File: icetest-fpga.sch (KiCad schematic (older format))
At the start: 26 parts, among them J1 R, J2 R, J3 R

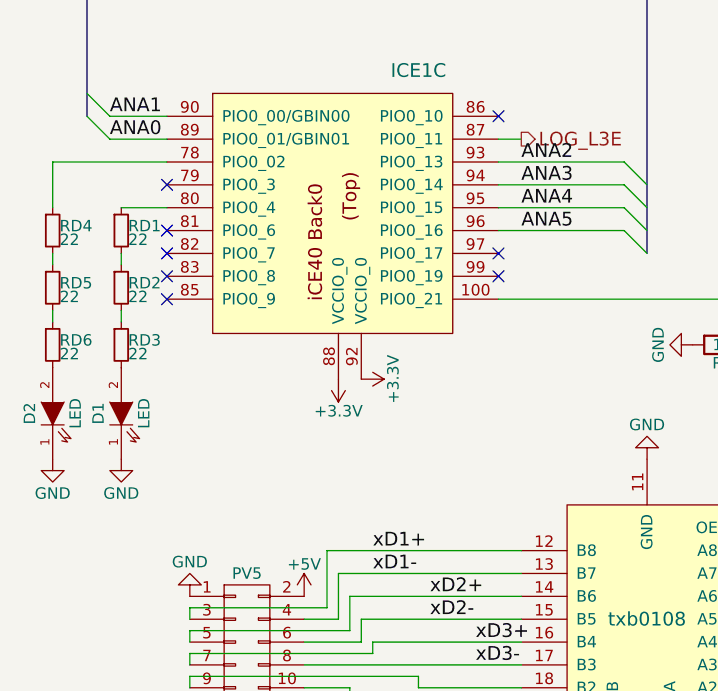
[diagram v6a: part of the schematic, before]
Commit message: more current for LEDs
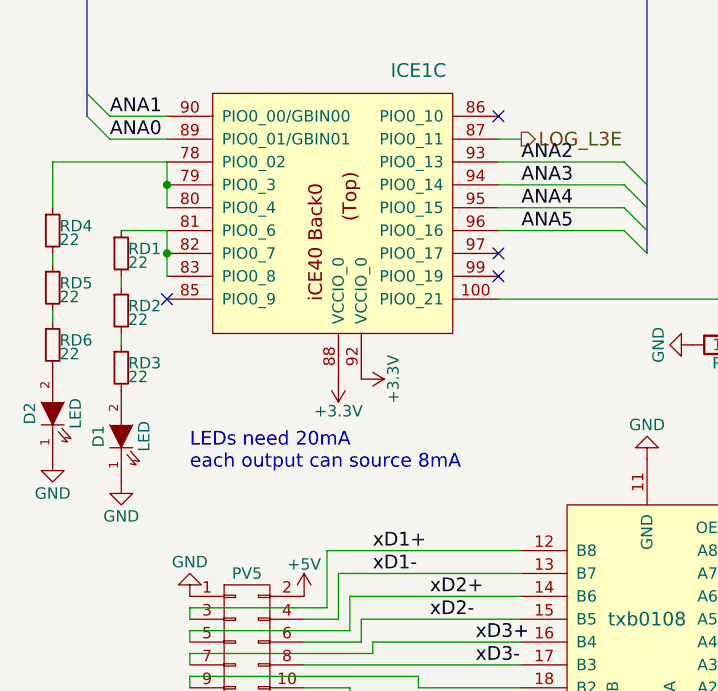
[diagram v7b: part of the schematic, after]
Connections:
- net at ICE1.78 (PIO0_02), RD4.1: now also ICE1.79 (PIO0_3), ICE1.80 (PIO0_4)
- net at RD1.1: now also ICE1.81 (PIO0_6), ICE1.82 (PIO0_7), ICE1.83 (PIO0_8); no longer ICE1.80 (PIO0_4)
- no-connect marks 31 -> 27
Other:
- note added: "LEDs need 20mA\neach output can source 8mA"
- moved on the sheet: D1, RD1, RD2, RD3
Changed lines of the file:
@@
 NoConn ~ 2650 4300
 NoConn ~ 2650 4400
-NoConn ~ 1200 4000
-NoConn ~ 1200 4200
-NoConn ~ 1200 4300
 NoConn ~ 1200 4500
 Text Label 6200 5400 0    60   ~ 0
@@
 	4700 2300 4950 2300
 NoConn ~ 6400 3350
-NoConn ~ 1200 4400
 Wire Wire Line
 	2750 3800 2650 3800
@@
 L LED D1
 U 1 1 578DAD29
-P 1000 5000
-F 0 "D1" H 1000 5100 50  0000 C CNN
-F 1 "LED" H 1000 4900 50  0000 C CNN
-F 2 "local:D_0603_HandSoldering" H 1000 5000 50  0001 C CNN
-F 3 "" H 1000 5000 50  0000 C CNN
-	1    1000 5000
+P 1000 5100
+F 0 "D1" H 1000 5200 50  0000 C CNN
+F 1 "LED" H 1000 5000 50  0000 C CNN
+F 2 "local:D_0603_HandSoldering" H 1000 5100 50  0001 C CNN
+F 3 "" H 1000 5100 50  0000 C CNN
+	1    1000 5100
 	0    -1   -1   0
 $EndComp
@@
 L GND #PWR072
 U 1 1 578DB32E
-P 1000 5200
-F 0 "#PWR072" H 1000 4950 50  0001 C CNN
-F 1 "GND" H 1000 5050 50  0000 C CNN
-F 2 "" H 1000 5200 50  0000 C CNN
-F 3 "" H 1000 5200 50  0000 C CNN
-	1    1000 5200
-	1    0    0    -1
-$EndComp
-Wire Wire Line
-	1200 4100 1000 4100
-Wire Wire Line
-	1000 4600 1000 4550
-Wire Wire Line
-	1000 4350 1000 4300
+P 1000 5300
+F 0 "#PWR072" H 1000 5050 50  0001 C CNN
+F 1 "GND" H 1000 5150 50  0000 C CNN
+F 2 "" H 1000 5300 50  0000 C CNN
+F 3 "" H 1000 5300 50  0000 C CNN
+	1    1000 5300
+	1    0    0    -1
+$EndComp
+Wire Wire Line
+	1000 4700 1000 4650
+Wire Wire Line
+	1000 4450 1000 4400
 $Comp
 L R_Small RD2
 U 1 1 578DAF76
-P 1000 4450
-F 0 "RD2" H 1030 4470 50  0000 L CNN
-F 1 "22" H 1030 4410 50  0000 L CNN
-F 2 "Resistors_SMD:R_0603_HandSoldering" H 1000 4450 50  0001 C CNN
-F 3 "" H 1000 4450 50  0000 C CNN
-	1    1000 4450
+P 1000 4550
+F 0 "RD2" H 1030 4570 50  0000 L CNN
+F 1 "22" H 1030 4510 50  0000 L CNN
+F 2 "Resistors_SMD:R_0603_HandSoldering" H 1000 4550 50  0001 C CNN
+F 3 "" H 1000 4550 50  0000 C CNN
+	1    1000 4550
 	1    0    0    -1
 $EndComp
@@
 L R_Small RD3
 U 1 1 578DAFC3
-P 1000 4700
-F 0 "RD3" H 1030 4720 50  0000 L CNN
-F 1 "22" H 1030 4660 50  0000 L CNN
-F 2 "Resistors_SMD:R_0603_HandSoldering" H 1000 4700 50  0001 C CNN
-F 3 "" H 1000 4700 50  0000 C CNN
-	1    1000 4700
+P 1000 4800
+F 0 "RD3" H 1030 4820 50  0000 L CNN
+F 1 "22" H 1030 4760 50  0000 L CNN
+F 2 "Resistors_SMD:R_0603_HandSoldering" H 1000 4800 50  0001 C CNN
+F 3 "" H 1000 4800 50  0000 C CNN
+	1    1000 4800
 	1    0    0    -1
 $EndComp
@@
 L R_Small RD1
 U 1 1 578DAE6A
-P 1000 4200
-F 0 "RD1" H 1030 4220 50  0000 L CNN
-F 1 "22" H 1030 4160 50  0000 L CNN
-F 2 "Resistors_SMD:R_0603_HandSoldering" H 1000 4200 50  0001 C CNN
-F 3 "" H 1000 4200 50  0000 C CNN
-	1    1000 4200
+P 1000 4300
+F 0 "RD1" H 1030 4320 50  0000 L CNN
+F 1 "22" H 1030 4260 50  0000 L CNN
+F 2 "Resistors_SMD:R_0603_HandSoldering" H 1000 4300 50  0001 C CNN
+F 3 "" H 1000 4300 50  0000 C CNN
+	1    1000 4300
 	1    0    0    -1
 $EndComp
@@
 Wire Bus Line
 	850  3100 850  3700
+Wire Wire Line
+	1200 3900 1200 4100
+Connection ~ 1200 4000
+Wire Wire Line
+	1200 4200 1000 4200
+Wire Wire Line
+	1200 4200 1200 4400
+Connection ~ 1200 4300
+Text Notes 1300 5250 0    60   ~ 0
+LEDs need 20mA\neach output can source 8mA
 $EndSCHEMATC

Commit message: minor layout
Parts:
- removed J1, J2, J3: R, Resistors_SMD:R_0603_HandSoldering, symbol R
- added W4: CDONE, Connect:PINTST, symbol TEST_1P
- added W5: RST, Connect:PINTST, symbol TEST_1P
- W1: value TEST_1P -> SCLK
- W2: value TEST_1P -> MISO
- W3: value TEST_1P -> MOSI
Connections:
- net ICE_CDONE: now also W4.1
- net ICE_RST: now also W5.1
- net MISO: now also W2.1; no longer W3.1
- net MOSI: now also W3.1; no longer W2.1
- no-connect marks 27 -> 30
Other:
- note removed: "2nd SPI for\nuser logic"
- moved on the sheet: RCLK1, W1, W2, W3
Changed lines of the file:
@@
 Text HLabel 8050 1550 2    60   Output ~ 0
 MISO
-Text HLabel 8050 1650 2    60   Input ~ 0
+Text HLabel 8550 1650 2    60   Input ~ 0
 MOSI
-Text HLabel 8600 1750 2    60   Input ~ 0
+Text HLabel 9150 1750 2    60   Input ~ 0
 SCK
 Text HLabel 9150 1850 2    60   Input ~ 0
@@
 	7650 1550 8050 1550
 Wire Wire Line
-	8050 1650 7650 1650
-Wire Wire Line
-	7650 1750 8600 1750
+	8550 1650 7650 1650
+Wire Wire Line
+	7650 1750 9150 1750
 Wire Wire Line
 	7650 1850 9150 1850
@@
 Wire Wire Line
 	2000 6200 1800 6200
-Wire Wire Line
-	6150 3450 6400 3450
-Wire Wire Line
-	6150 3550 6400 3550
-Wire Wire Line
-	6150 3650 6400 3650
-Text Label 5600 3450 0    60   ~ 0
-SCK
-Text Label 5600 3550 0    60   ~ 0
-MOSI
-Text Label 5600 3650 0    60   ~ 0
-MISO
-Text Notes 5600 3900 0    60   ~ 0
-2nd SPI for\nuser logic
 $Comp
 L iCE40HX1K-VQ100 ICE1
@@
 	8900 1950 8900 1850
 Connection ~ 8900 1850
-Text Notes 8400 2650 0    60   ~ 0
+Text Notes 9100 2450 0    60   ~ 0
 SS low chooses SPI slave\nconfig mode.
 $Comp
 L TEST_1P W1
 U 1 1 5793C294
-P 8800 1100
-F 0 "W1" H 8800 1300 50  0000 C CNN
-F 1 "TEST_1P" H 8800 1300 50  0001 C CNN
-F 2 "Connect:PINTST" H 9000 1100 50  0001 C CNN
-F 3 "" H 9000 1100 50  0000 C CNN
-	1    8800 1100
+P 9100 1700
+F 0 "W1" H 9100 1900 50  0000 C CNN
+F 1 "SCLK" H 9100 1900 50  0001 C CNN
+F 2 "Connect:PINTST" H 9300 1700 50  0001 C CNN
+F 3 "" H 9300 1700 50  0000 C CNN
+	1    9100 1700
 	1    0    0    -1
 $EndComp
@@
 L TEST_1P W2
 U 1 1 5793C65E
-P 8950 1100
-F 0 "W2" H 8950 1300 50  0000 C CNN
-F 1 "TEST_1P" H 8950 1300 50  0001 C CNN
-F 2 "Connect:PINTST" H 9150 1100 50  0001 C CNN
-F 3 "" H 9150 1100 50  0000 C CNN
-	1    8950 1100
+P 7950 1450
+F 0 "W2" H 7950 1650 50  0000 C CNN
+F 1 "MISO" H 7950 1650 50  0001 C CNN
+F 2 "Connect:PINTST" H 8150 1450 50  0001 C CNN
+F 3 "" H 8150 1450 50  0000 C CNN
+	1    7950 1450
 	1    0    0    -1
 $EndComp
@@
 L TEST_1P W3
 U 1 1 5793C6B3
-P 9100 1100
-F 0 "W3" H 9100 1300 50  0000 C CNN
-F 1 "TEST_1P" H 9100 1300 50  0001 C CNN
-F 2 "Connect:PINTST" H 9300 1100 50  0001 C CNN
-F 3 "" H 9300 1100 50  0000 C CNN
-	1    9100 1100
-	1    0    0    -1
-$EndComp
-Text HLabel 8800 1100 3    60   Input ~ 0
-SCK
-Text HLabel 8950 1100 3    60   Input ~ 0
-MOSI
-Text HLabel 9100 1100 3    60   Output ~ 0
-MISO
+P 8450 1550
+F 0 "W3" H 8450 1750 50  0000 C CNN
+F 1 "MOSI" H 8450 1750 50  0001 C CNN
+F 2 "Connect:PINTST" H 8650 1550 50  0001 C CNN
+F 3 "" H 8650 1550 50  0000 C CNN
+	1    8450 1550
+	1    0    0    -1
+$EndComp
 Wire Bus Line
 	5050 1200 5050 2400
@@
 Entry Wire Line
 	4950 2300 5050 2400
-$Comp
-L R J1
-U 1 1 5796B92D
-P 6000 3450
-F 0 "J1" V 6000 3450 50  0000 C CNN
-F 1 "R" H 6000 3450 50  0001 C CNN
-F 2 "Resistors_SMD:R_0603_HandSoldering" V 5930 3450 50  0001 C CNN
-F 3 "" H 6000 3450 50  0000 C CNN
-	1    6000 3450
-	0    1    1    0
-$EndComp
-$Comp
-L R J2
-U 1 1 5796BB7A
-P 6000 3550
-F 0 "J2" V 6000 3550 50  0000 C CNN
-F 1 "R" H 6000 3550 50  0001 C CNN
-F 2 "Resistors_SMD:R_0603_HandSoldering" V 5930 3550 50  0001 C CNN
-F 3 "" H 6000 3550 50  0000 C CNN
-	1    6000 3550
-	0    1    1    0
-$EndComp
-$Comp
-L R J3
-U 1 1 5796BBD2
-P 6000 3650
-F 0 "J3" V 6000 3650 50  0000 C CNN
-F 1 "R" H 6000 3650 50  0001 C CNN
-F 2 "Resistors_SMD:R_0603_HandSoldering" V 5930 3650 50  0001 C CNN
-F 3 "" H 6000 3650 50  0000 C CNN
-	1    6000 3650
-	0    1    1    0
-$EndComp
-Wire Wire Line
-	5850 3450 5600 3450
-Wire Wire Line
-	5600 3550 5850 3550
-Wire Wire Line
-	5850 3650 5600 3650
 $Comp
 L +3.3V #PWR074
@@
 L R RCLK1
 U 1 1 57A6985B
-P 8500 1400
-F 0 "RCLK1" V 8580 1400 50  0000 C CNN
-F 1 "10k" V 8500 1400 50  0000 C CNN
-F 2 "Resistors_SMD:R_0603_HandSoldering" V 8430 1400 50  0001 C CNN
-F 3 "" H 8500 1400 50  0000 C CNN
-	1    8500 1400
+P 8900 1400
+F 0 "RCLK1" V 8980 1400 50  0000 C CNN
+F 1 "10k" V 8900 1400 50  0000 C CNN
+F 2 "Resistors_SMD:R_0603_HandSoldering" V 8830 1400 50  0001 C CNN
+F 3 "" H 8900 1400 50  0000 C CNN
+	1    8900 1400
 	1    0    0    -1
 $EndComp
@@
 L +3.3V #PWR076
 U 1 1 57A698FC
-P 8500 1250
-F 0 "#PWR076" H 8500 1100 50  0001 C CNN
-F 1 "+3.3V" H 8500 1390 50  0000 C CNN
-F 2 "" H 8500 1250 50  0000 C CNN
-F 3 "" H 8500 1250 50  0000 C CNN
-	1    8500 1250
-	1    0    0    -1
-$EndComp
-Wire Wire Line
-	8500 1550 8500 1750
-Connection ~ 8500 1750
+P 8900 1250
+F 0 "#PWR076" H 8900 1100 50  0001 C CNN
+F 1 "+3.3V" H 8900 1390 50  0000 C CNN
+F 2 "" H 8900 1250 50  0000 C CNN
+F 3 "" H 8900 1250 50  0000 C CNN
+	1    8900 1250
+	1    0    0    -1
+$EndComp
+Wire Wire Line
+	8900 1550 8900 1750
+Connection ~ 8900 1750
 Entry Wire Line
 	2900 2100 3000 2200
@@
 $EndComp
 $Comp
-L GND #PWR?
+L GND #PWR077
 U 1 1 57A7141F
 P 700 5200
-F 0 "#PWR?" H 700 4950 50  0001 C CNN
+F 0 "#PWR077" H 700 4950 50  0001 C CNN
 F 1 "GND" H 700 5050 50  0000 C CNN
 F 2 "" H 700 5200 50  0000 C CNN
@@
 Text Notes 1300 5250 0    60   ~ 0
 LEDs need 20mA\neach output can source 8mA
+NoConn ~ 6400 3450
+NoConn ~ 6400 3550
+NoConn ~ 6400 3650
+Wire Wire Line
+	7950 1450 7950 1550
+Connection ~ 7950 1550
+Wire Wire Line
+	8450 1550 8450 1650
+Connection ~ 8450 1650
+Wire Wire Line
+	9100 1700 9100 1750
+Connection ~ 9100 1750
+$Comp
+L TEST_1P W5
+U 1 1 57A7D34E
+P 7650 2300
+F 0 "W5" H 7650 2500 50  0000 C CNN
+F 1 "RST" H 7650 2500 50  0001 C CNN
+F 2 "Connect:PINTST" H 7850 2300 50  0001 C CNN
+F 3 "" H 7850 2300 50  0000 C CNN
+	1    7650 2300
+	-1   0    0    1
+$EndComp
+$Comp
+L TEST_1P W4
+U 1 1 57A7D3FD
+P 8250 2350
+F 0 "W4" H 8250 2550 50  0000 C CNN
+F 1 "CDONE" H 8250 2550 50  0001 C CNN
+F 2 "Connect:PINTST" H 8450 2350 50  0001 C CNN
+F 3 "" H 8450 2350 50  0000 C CNN
+	1    8250 2350
+	-1   0    0    1
+$EndComp
 $EndSCHEMATC
